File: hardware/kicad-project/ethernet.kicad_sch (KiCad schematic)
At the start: 42 parts, among them IC6 IC_ETH_PHY_LAN8742A, J8 J_RJ45_SKT_MAG_LED, Y2 25MHZ

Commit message: Added extra pins for external switching
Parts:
- FB1: footprint Inductor_SMD:L_0603_1608Metric_Pad1.05x0.95mm_HandSolder -> Inductor_SMD:L_0603_1608Metric
- IC6: footprint ebnx_footprints:LAN8750A_SQFN24 -> Package_DFN_QFN:VQFN-24-1EP_4x4mm_P0.5mm_EP2.5x2.5mm_ThermalVias
- Y2: footprint diseqc_cntrl:ABLS25000MHZDFT -> ebnx_footprints:ABLS25000MHZDFT
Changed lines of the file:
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@@
 			)
 		)
-		(property "Footprint" "diseqc_cntrl:ABLS25000MHZDFT"
+		(property "Footprint" "ebnx_footprints:ABLS25000MHZDFT"
 			(at 45.72 37.16 0)
 			(hide yes)
@@
 			)
 		)
-		(property "Footprint" "ebnx_footprints:LAN8750A_SQFN24"
+		(property "Footprint" "Package_DFN_QFN:VQFN-24-1EP_4x4mm_P0.5mm_EP2.5x2.5mm_ThermalVias"
 			(at 119.38 173.66 0)
 			(hide yes)
@@
 			)
 		)
-		(property "Footprint" "Inductor_SMD:L_0603_1608Metric_Pad1.05x0.95mm_HandSolder"
+		(property "Footprint" "Inductor_SMD:L_0603_1608Metric"
 			(at 165.862 53.34 90)
 			(hide yes)

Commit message: Removed hand solder pads
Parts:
- C30, C31, C32, C33, C34, C35, C36, C37: footprint Capacitor_SMD:C_0603_1608Metric_Pad1.08x0.95mm_HandSolder -> Capacitor_SMD:C_0603_1608Metric
- R20, R21, R22, R23, R24, R25, R26, R27, R28, R29, R30, R31, R32, R33, R34, R35, R36, R37, R38, R39: footprint Resistor_SMD:R_0603_1608Metric_Pad0.98x0.95mm_HandSolder -> Resistor_SMD:R_0603_1608Metric
- TP15, TP16, TP17, TP18, TP19, TP20, TP21, TP22, TP24: now left out of the parts list
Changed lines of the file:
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@@
 		(body_style 1)
 		(exclude_from_sim no)
-		(in_bom yes)
+		(in_bom no)
 		(on_board yes)
 		(in_pos_files yes)
@@
 			)
 		)
-		(property "Footprint" "Capacitor_SMD:C_0603_1608Metric_Pad1.08x0.95mm_HandSolder"
+		(property "Footprint" "Capacitor_SMD:C_0603_1608Metric"
 			(at 38.4048 138.43 0)
 			(hide yes)
@@
 			)
 		)
-		(property "Footprint" "Resistor_SMD:R_0603_1608Metric_Pad0.98x0.95mm_HandSolder"
+		(property "Footprint" "Resistor_SMD:R_0603_1608Metric"
 			(at 44.45 109.728 90)
 			(hide yes)
@@
 			)
 		)
-		(property "Footprint" "Resistor_SMD:R_0603_1608Metric_Pad0.98x0.95mm_HandSolder"
+		(property "Footprint" "Resistor_SMD:R_0603_1608Metric"
 			(at 130.81 103.378 90)
 			(hide yes)
@@
 			)
 		)
-		(property "Footprint" "Resistor_SMD:R_0603_1608Metric_Pad0.98x0.95mm_HandSolder"
+		(property "Footprint" "Resistor_SMD:R_0603_1608Metric"
 			(at 149.352 64.77 90)
 			(hide yes)
@@
 			)
 		)
-		(property "Footprint" "Resistor_SMD:R_0603_1608Metric_Pad0.98x0.95mm_HandSolder"
+		(property "Footprint" "Resistor_SMD:R_0603_1608Metric"
 			(at 156.972 64.77 90)
 			(hide yes)
@@
 			)
 		)
-		(property "Footprint" "Resistor_SMD:R_0603_1608Metric_Pad0.98x0.95mm_HandSolder"
+		(property "Footprint" "Resistor_SMD:R_0603_1608Metric"
 			(at 134.112 64.77 90)
 			(hide yes)
@@
 			)
 		)
-		(property "Footprint" "Resistor_SMD:R_0603_1608Metric_Pad0.98x0.95mm_HandSolder"
+		(property "Footprint" "Resistor_SMD:R_0603_1608Metric"
 			(at 258.572 104.14 90)
 			(hide yes)
@@
 		(body_style 1)
 		(exclude_from_sim no)
-		(in_bom yes)
+		(in_bom no)
 		(on_board yes)
 		(in_pos_files yes)
@@
 			)
 		)
-		(property "Footprint" "Capacitor_SMD:C_0603_1608Metric_Pad1.08x0.95mm_HandSolder"
+		(property "Footprint" "Capacitor_SMD:C_0603_1608Metric"
 			(at 147.0152 134.62 0)
 			(hide yes)
@@
 		(body_style 1)
 		(exclude_from_sim no)
-		(in_bom yes)
+		(in_bom no)
 		(on_board yes)
 		(in_pos_files yes)
@@
 			)
 		)
-		(property "Footprint" "Resistor_SMD:R_0603_1608Metric_Pad0.98x0.95mm_HandSolder"
+		(property "Footprint" "Resistor_SMD:R_0603_1608Metric"
 			(at 33.02 91.948 90)
 			(hide yes)
@@
 			)
 		)
-		(property "Footprint" "Capacitor_SMD:C_0603_1608Metric_Pad1.08x0.95mm_HandSolder"
+		(property "Footprint" "Capacitor_SMD:C_0603_1608Metric"
 			(at 59.9948 138.43 0)
 			(hide yes)
@@
 			)
 		)
-		(property "Footprint" "Capacitor_SMD:C_0603_1608Metric_Pad1.08x0.95mm_HandSolder"
+		(property "Footprint" "Capacitor_SMD:C_0603_1608Metric"
 			(at 173.6852 127 0)
 			(hide yes)
@@
 			)
 		)
-		(property "Footprint" "Resistor_SMD:R_0603_1608Metric_Pad0.98x0.95mm_HandSolder"
+		(property "Footprint" "Resistor_SMD:R_0603_1608Metric"
 			(at 33.02 114.808 90)
 			(hide yes)
@@
 			)
 		)
-		(property "Footprint" "Resistor_SMD:R_0603_1608Metric_Pad0.98x0.95mm_HandSolder"
+		(property "Footprint" "Resistor_SMD:R_0603_1608Metric"
 			(at 33.02 86.868 90)
 			(hide yes)
@@
 			)
 		)
-		(property "Footprint" "Resistor_SMD:R_0603_1608Metric_Pad0.98x0.95mm_HandSolder"
+		(property "Footprint" "Resistor_SMD:R_0603_1608Metric"
 			(at 33.02 100.838 90)
 			(hide yes)
@@
 			)
 		)
-		(property "Footprint" "Resistor_SMD:R_0603_1608Metric_Pad0.98x0.95mm_HandSolder"
+		(property "Footprint" "Resistor_SMD:R_0603_1608Metric"
 			(at 33.02 84.328 90)
 			(hide yes)
@@
 			)
 		)
-		(property "Footprint" "Capacitor_SMD:C_0603_1608Metric_Pad1.08x0.95mm_HandSolder"
+		(property "Footprint" "Capacitor_SMD:C_0603_1608Metric"
 			(at 127.9652 120.65 0)
 			(hide yes)
@@
 			)
 		)
-		(property "Footprint" "Resistor_SMD:R_0603_1608Metric_Pad0.98x0.95mm_HandSolder"
+		(property "Footprint" "Resistor_SMD:R_0603_1608Metric"
 			(at 249.682 104.14 90)
 			(hide yes)
@@
 			)
 		)
-		(property "Footprint" "Resistor_SMD:R_0603_1608Metric_Pad0.98x0.95mm_HandSolder"
+		(property "Footprint" "Resistor_SMD:R_0603_1608Metric"
 			(at 271.018 104.14 90)
 			(hide yes)
@@
 			)
 		)
-		(property "Footprint" "Resistor_SMD:R_0603_1608Metric_Pad0.98x0.95mm_HandSolder"
+		(property "Footprint" "Resistor_SMD:R_0603_1608Metric"
 			(at 50.292 68.58 90)
 			(hide yes)
@@
 		(body_style 1)
 		(exclude_from_sim no)
-		(in_bom yes)
+		(in_bom no)
 		(on_board yes)
 		(in_pos_files yes)
@@
 			)
 		)
-		(property "Footprint" "Resistor_SMD:R_0603_1608Metric_Pad0.98x0.95mm_HandSolder"
+		(property "Footprint" "Resistor_SMD:R_0603_1608Metric"
 			(at 33.02 94.488 90)
 			(hide yes)
@@
 		(body_style 1)
 		(exclude_from_sim no)
-		(in_bom yes)
+		(in_bom no)
 		(on_board yes)
 		(in_pos_files yes)
@@
 			)
 		)
-		(property "Footprint" "Resistor_SMD:R_0603_1608Metric_Pad0.98x0.95mm_HandSolder"
+		(property "Footprint" "Resistor_SMD:R_0603_1608Metric"
 			(at 46.482 68.58 90)
 			(hide yes)
@@
 			)
 		)
-		(property "Footprint" "Resistor_SMD:R_0603_1608Metric_Pad0.98x0.95mm_HandSolder"
+		(property "Footprint" "Resistor_SMD:R_0603_1608Metric"
 			(at 141.732 64.77 90)
 			(hide yes)
@@
 			)
 		)
-		(property "Footprint" "Resistor_SMD:R_0603_1608Metric_Pad0.98x0.95mm_HandSolder"
+		(property "Footprint" "Resistor_SMD:R_0603_1608Metric"
 			(at 44.45 118.618 90)
 			(hide yes)
@@
 		(body_style 1)
 		(exclude_from_sim no)
-		(in_bom yes)
+		(in_bom no)
 		(on_board yes)
 		(in_pos_files yes)
@@
 		(body_style 1)
 		(exclude_from_sim no)
-		(in_bom yes)
+		(in_bom no)
 		(on_board yes)
 		(in_pos_files yes)
@@
 		(body_style 1)
 		(exclude_from_sim no)
-		(in_bom yes)
+		(in_bom no)
 		(on_board yes)
 		(in_pos_files yes)
@@
 			)
 		)
-		(property "Footprint" "Capacitor_SMD:C_0603_1608Metric_Pad1.08x0.95mm_HandSolder"
+		(property "Footprint" "Capacitor_SMD:C_0603_1608Metric"
 			(at 166.0652 135.89 0)
 			(hide yes)
@@
 			)
 		)
-		(property "Footprint" "Capacitor_SMD:C_0603_1608Metric_Pad1.08x0.95mm_HandSolder"
+		(property "Footprint" "Capacitor_SMD:C_0603_1608Metric"
 			(at 140.6652 134.62 0)
 			(hide yes)
@@
 			)
 		)
-		(property "Footprint" "Capacitor_SMD:C_0603_1608Metric_Pad1.08x0.95mm_HandSolder"
+		(property "Footprint" "Capacitor_SMD:C_0603_1608Metric"
 			(at 178.7652 135.89 0)
 			(hide yes)
@@
 			)
 		)
-		(property "Footprint" "Resistor_SMD:R_0603_1608Metric_Pad0.98x0.95mm_HandSolder"
+		(property "Footprint" "Resistor_SMD:R_0603_1608Metric"
 			(at 42.672 68.58 90)
 			(hide yes)
@@
 		(body_style 1)
 		(exclude_from_sim no)
-		(in_bom yes)
+		(in_bom no)
 		(on_board yes)
 		(in_pos_files yes)
@@
 			)
 		)
-		(property "Footprint" "Resistor_SMD:R_0603_1608Metric_Pad0.98x0.95mm_HandSolder"
+		(property "Footprint" "Resistor_SMD:R_0603_1608Metric"
 			(at 33.02 97.028 90)
 			(hide yes)

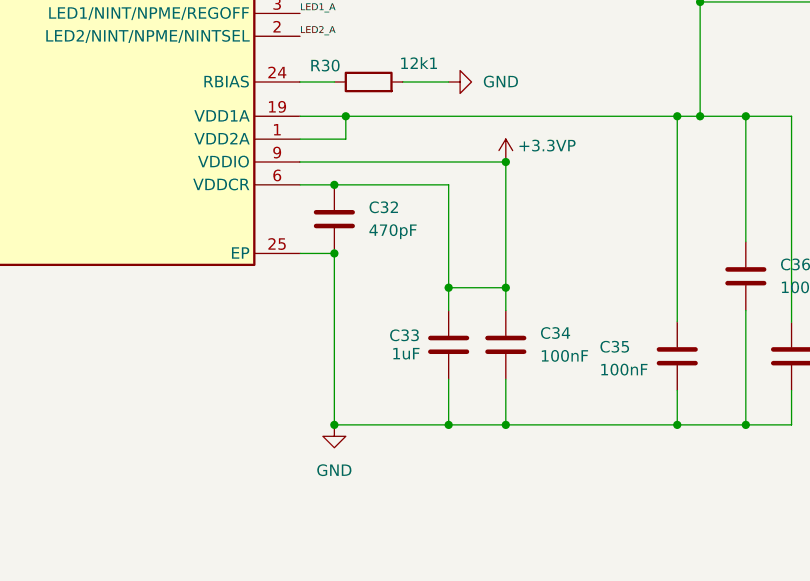
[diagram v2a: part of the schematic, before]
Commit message: Bugfix: IC6 pin 6 incorrectly connected to 3v3
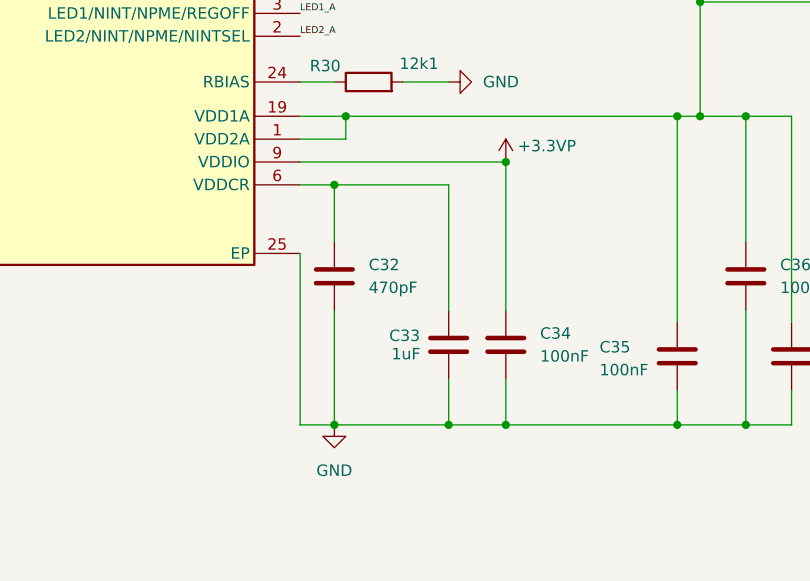
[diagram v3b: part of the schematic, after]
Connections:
- net +3.3VP: no longer C32.1, C33.1, IC6.6 (VDDCR)
- new net: C32.1, C33.1, IC6.6 (VDDCR)
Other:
- moved on the sheet: C32
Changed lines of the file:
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@@
 	(paper "A4")
 	(junction
-		(at 146.05 124.46)
-		(diameter 0)
-		(color 0 0 0 0)
-	)
-	(junction
 		(at 48.26 60.96)
 		(diameter 0)
@@
 	)
 	(junction
-		(at 127 113.03)
-		(diameter 0)
-		(color 0 0 0 0)
-	)
-	(junction
 		(at 59.69 90.17)
 		(diameter 0)
@@
 	)
 	(junction
+		(at 127 113.03)
+		(diameter 0)
+		(color 0 0 0 0)
+	)
+	(junction
 		(at 55.88 104.14)
 		(diameter 0)
@@
 	)
 	(junction
-		(at 139.7 124.46)
-		(diameter 0)
-		(color 0 0 0 0)
-	)
-	(junction
 		(at 167.64 92.71)
 		(diameter 0)
@@
 		(color 0 0 0 0)
 	)
-	(junction
-		(at 127 120.65)
-		(diameter 0)
-		(color 0 0 0 0)
-	)
 	(bus_entry
 		(at 15.24 110.49)
@@
 	(wire
 		(pts
-			(xy 139.7 124.46) (xy 146.05 124.46)
-		)
-		(stroke
-			(width 0)
-			(type default)
-		)
-	)
-	(wire
-		(pts
 			(xy 203.2 87.63) (xy 208.28 87.63)
 		)
@@
 	(wire
 		(pts
-			(xy 139.7 127) (xy 139.7 124.46)
-		)
-		(stroke
-			(width 0)
-			(type default)
-		)
-	)
-	(wire
-		(pts
 			(xy 26.67 99.06) (xy 29.21 99.06)
 		)
@@
 	(wire
 		(pts
+			(xy 123.19 139.7) (xy 123.19 120.65)
+		)
+		(stroke
+			(width 0)
+			(type default)
+		)
+	)
+	(wire
+		(pts
 			(xy 17.78 19.05) (xy 24.13 19.05)
 		)
@@
 	(wire
 		(pts
-			(xy 146.05 110.49) (xy 146.05 124.46)
+			(xy 146.05 110.49) (xy 146.05 127)
 		)
 		(stroke
@@
 		)
 	)
-	(wire
-		(pts
-			(xy 146.05 124.46) (xy 146.05 127)
-		)
-		(stroke
-			(width 0)
-			(type default)
-		)
-	)
 	(bus
 		(pts
@@
 	(wire
 		(pts
-			(xy 123.19 120.65) (xy 127 120.65)
+			(xy 123.19 139.7) (xy 127 139.7)
 		)
 		(stroke
@@
 	(wire
 		(pts
-			(xy 127 139.7) (xy 127 120.65)
+			(xy 127 139.7) (xy 127 127)
 		)
 		(stroke
@@
 	(wire
 		(pts
-			(xy 139.7 113.03) (xy 139.7 124.46)
+			(xy 139.7 113.03) (xy 139.7 127)
 		)
 		(stroke
@@
 	(wire
 		(pts
+			(xy 127 119.38) (xy 127 113.03)
+		)
+		(stroke
+			(width 0)
+			(type default)
+		)
+	)
+	(wire
+		(pts
 			(xy 127 113.03) (xy 139.7 113.03)
 		)
@@
 	(symbol
 		(lib_id "#InvenTree:C_470p_0603")
-		(at 127 116.84 0)
+		(at 127 123.19 0)
 		(unit 1)
 		(body_style 1)
@@
 		(fields_autoplaced yes)
 		(property "Reference" "C32"
-			(at 130.81 115.5699 0)
+			(at 130.81 121.9199 0)
 			(show_name no)
 			(do_not_autoplace no)
@@
 		)
 		(property "Value" "470pF"
-			(at 130.81 118.1099 0)
+			(at 130.81 124.4599 0)
 			(show_name no)
 			(do_not_autoplace no)
@@
 		)
 		(property "Footprint" "Capacitor_SMD:C_0603_1608Metric"
-			(at 127.9652 120.65 0)
+			(at 127.9652 127 0)
 			(hide yes)
 			(show_name no)
@@
 		)
 		(property "Datasheet" ""
-			(at 127 116.84 0)
+			(at 127 123.19 0)
 			(hide yes)
 			(show_name no)
@@
 		)
 		(property "Description" ""
-			(at 127 116.84 0)
+			(at 127 123.19 0)
 			(hide yes)
 			(show_name no)
@@
 		)
 		(property "InvenTree" "253"
-			(at 127 116.84 0)
+			(at 127 123.19 0)
 			(hide yes)
 			(show_name no)
@@
 		)
 		(property "Part URL" "https://inventree.ebnx.net/web/part/253/"
-			(at 127 116.84 0)
+			(at 127 123.19 0)
 			(hide yes)
 			(show_name no)
@@
 		)
 		(property "InvenTree Part" "C_470p_0603"
-			(at 127 116.84 0)
+			(at 127 123.19 0)
 			(hide yes)
 			(show_name no)

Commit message: Renumbered/annotated
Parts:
- renumbered C30 to C37, C31 to C38, C32 to C39, C33 to C40, C34 to C41, C35 to C42, C36 to C43, C37 to C44, FB1 to FB2, IC6 to IC7, J8 to J9, R38 to R18, R39 to R19, TP15 to TP16, TP20 to TP17, TP21 to TP18, TP22 to TP19, TP24 to TP20, TP16 to TP21, TP17 to TP22, TP18 to TP23, TP19 to TP24
